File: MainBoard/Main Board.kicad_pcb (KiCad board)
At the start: 2 copper layers, 120 x 107 mm, 33 parts, among them IC1 TLV61070ADBVR, J1 Motor, J2 Motor, J3 Row 2, J4 Row 2, J8 Conn_01x16_Pin, Q1 NMOS, Q2 NMOS, U1 TP4056, U2 DW01A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

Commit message: Small Changes to mainboard schematic
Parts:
- removed C1, C2: 220u, Capacitor_THT:CP_Radial_D8.0mm_P5.00mm
- removed D5, D6: D, Diode_THT:D_DO-15_P10.16mm_Horizontal
- removed IC1: TLV61070ADBVR, ImportedLibrary:TLV61070ADBVR
- removed J2: Motor, TerminalBlock:TerminalBlock_bornier-2_P5.08mm
- removed L1: 4u7, Inductor_SMD:L_6.3x6.3_H3
- removed Q1, Q2: NMOS, Package_TO_SOT_THT:TO-220F-3_Vertical
- removed R1, R4, R9: 100, Resistor_SMD:R_0402_1005Metric
- removed R10, R2: 10k, Resistor_SMD:R_0402_1005Metric
- removed U1: TP4056, Package_SO:SO-8_3.9x4.9mm_P1.27mm
- removed U2: DW01A, Package_TO_SOT_SMD:SOT-23-6
- removed U3: FS8205A, Package_TO_SOT_SMD:SOT-23-6

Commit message: Updated Mainboard
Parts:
- added C1: 220u, Capacitor_THT:CP_Radial_D8.0mm_P5.00mm, F.Cu at (40.6, 99.0)
- added C10: 3n3, Capacitor_SMD:C_0402_1005Metric, F.Cu at (43.6, 124.2)
- added C11: 10u, Capacitor_SMD:C_0603_1608Metric, F.Cu at (40.2, 119.6)
- added C12: 10u, Capacitor_SMD:C_0603_1608Metric, F.Cu at (40.2, 122.1)
- added C13: 10u, Capacitor_SMD:C_0603_1608Metric, F.Cu at (40.2, 124.6)
- added C14: 2n2, Capacitor_SMD:C_0402_1005Metric, F.Cu at (43.6, 126.1)
- added C15: 10u, Capacitor_SMD:C_0603_1608Metric, F.Cu at (40.2, 127.1)
- added C16: 10u, Capacitor_SMD:C_0603_1608Metric, F.Cu at (40.2, 129.6)
- added C2: 220u, Capacitor_THT:CP_Radial_D8.0mm_P5.00mm, F.Cu at (40.6, 108.6)
- added C3: 100n, Capacitor_SMD:C_0402_1005Metric, F.Cu at (43.6, 114.3)
- added C4: 100n, Capacitor_SMD:C_0402_1005Metric, F.Cu at (43.6, 116.3)
- added C5: 10u, Capacitor_SMD:C_0603_1608Metric, F.Cu at (40.2, 114.6)
- added C6: 100n, Capacitor_SMD:C_0402_1005Metric, F.Cu at (43.6, 118.3)
- added C7: 10u, Capacitor_SMD:C_0603_1608Metric, F.Cu at (40.2, 117.1)
- added C8: 1u, Capacitor_SMD:C_0402_1005Metric, F.Cu at (43.6, 120.2)
- added C9: 100n, Capacitor_SMD:C_0402_1005Metric, F.Cu at (43.6, 122.2)
- added D1: LED, LED_SMD:LED_0603_1608Metric, F.Cu at (73.6, 95.5)
- added D2: LED, LED_SMD:LED_0603_1608Metric, F.Cu at (73.6, 98.1)
- added D3: PMEG2010AEH, Diode_SMD:D_SOD-123F, F.Cu at (71.0, 116.2)
- added D4: PMEG2010AEH, Diode_SMD:D_SOD-123F, F.Cu at (71.0, 119.6)
- added D5: PMEG2010AEH, Diode_SMD:D_SOD-123F, F.Cu at (71.0, 122.9)
- added D6: PMEG2010AEH, Diode_SMD:D_SOD-123F, F.Cu at (71.0, 126.3)
- added IC1: TLV61070ADBVR, ImportedLibrary:TLV61070ADBVR, F.Cu at (44.8, 129.4)
- added J2: Motor, TerminalBlock:TerminalBlock_bornier-2_P5.08mm, F.Cu at (51.1, 119.1)
- added J5: USB PowerOnly 6P, Connector_USB:USB_C_Receptacle_GCT_USB4125-xx-x_6P_TopMnt_Horizontal, F.Cu at (65.6, 99.1)
- added L1: 6u8, Inductor_SMD:L_6.3x6.3_H3, F.Cu at (63.7, 128.4)
- added L2: 2u2, Inductor_SMD:L_Changjiang_FNR5030S, F.Cu at (73.5, 110.1)
- added Q1: NMOS, Package_TO_SOT_THT:TO-220F-3_Vertical, F.Cu at (51.3, 98.1)
- added Q2: NMOS, Package_TO_SOT_THT:TO-220F-3_Vertical, F.Cu at (51.3, 104.3)
- added R1: 100, Resistor_SMD:R_0402_1005Metric, F.Cu at (60.9, 115.5)
- added R10: 10k, Resistor_SMD:R_0402_1005Metric, F.Cu at (63.8, 123.5)
- added R11: R, Resistor_SMD:R_0402_1005Metric, F.Cu at (66.7, 115.5)
- added R12: R, Resistor_SMD:R_0402_1005Metric, F.Cu at (66.7, 117.5)
- added R13: 90k, Resistor_SMD:R_0402_1005Metric, F.Cu at (66.7, 119.5)
- added R14: 10k, Resistor_SMD:R_0402_1005Metric, F.Cu at (66.7, 121.5)
- added R2: 10k, Resistor_SMD:R_0402_1005Metric, F.Cu at (60.9, 117.5)
- added R3: 1k2, Resistor_SMD:R_0402_1005Metric, F.Cu at (60.9, 119.5)
- added R4: 100, Resistor_SMD:R_0402_1005Metric, F.Cu at (60.9, 121.5)
- added R5: 1k, Resistor_SMD:R_0402_1005Metric, F.Cu at (60.9, 123.5)
- added R6: 1k2, Resistor_SMD:R_0402_1005Metric, F.Cu at (63.8, 115.5)
- added R7: 1k2, Resistor_SMD:R_0402_1005Metric, F.Cu at (63.8, 117.5)
- added R8: 24k, Resistor_SMD:R_0402_1005Metric, F.Cu at (63.8, 119.5)
- added R9: 100, Resistor_SMD:R_0402_1005Metric, F.Cu at (63.8, 121.5)
- added RV1: R_Potentiometer, Potentiometer_SMD:Potentiometer_Bourns_TC33X_Vertical, F.Cu at (51.1, 126.0)
- added RV2: R_Potentiometer, Potentiometer_SMD:Potentiometer_Bourns_TC33X_Vertical, F.Cu at (51.1, 130.7)
- added SW1: SS12D10G5, ImportedLibrary:SS12D10G5_SlideSwitch, F.Cu at (54.8, 111.3)
- added U1: TP4056, Package_SO:SO-8_3.9x4.9mm_P1.27mm, F.Cu at (65.9, 110.0)
- added U2: DW01A, Package_TO_SOT_SMD:SOT-23-6, F.Cu at (56.6, 125.8)
- added U3: FS8205A, Package_TO_SOT_SMD:SOT-23-6, F.Cu at (56.6, 130.3)
- added U4: TPS61085DGK, Package_SO:VSSOP-8_3.0x3.0mm_P0.65mm, F.Cu at (72.2, 130.2)
- J8: value Conn_01x16_Pin -> FFC Connector
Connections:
- net /NANO_D10 renamed /PWM_L
- net /NANO_D9 renamed /PWM_R
- A1 pad 10: /NANO_D7 -> /IR_6_D
- A1 pad 11: /NANO_D8 -> /IR_7_D
- A1 pad 19: /NANO_A0 -> /IR_2_A
- A1 pad 20: /NANO_A1 -> /IR_3_A
- A1 pad 21: /NANO_A2 -> /IR_4_A
- A1 pad 22: /NANO_A3 -> /IR_5_A
- A1 pad 23: /NANO_A4 -> /IR_6_A
- A1 pad 30: +5V -> Net-(A1-VIN)
- A1 pad 5: /NANO_D2 -> /IR_1_D
- A1 pad 6: /NANO_D3 -> /IR_2_D
- A1 pad 7: /NANO_D4 -> /IR_3_D
- A1 pad 8: /NANO_D5 -> /IR_4_D
- A1 pad 9: /NANO_D6 -> /IR_5_D
- BT1 pad 1: +BATT -> Net-(BT1-+)
- BT1 pad 2: -BATT -> Net-(BT1--)
- J1 pad 1: VBUS -> Vdrive
- J3 pad 10: /NANO_D7 -> /IR_6_D
- J3 pad 11: /NANO_D8 -> /IR_7_D
- J3 pad 5: /NANO_D2 -> /IR_1_D
- J3 pad 6: /NANO_D3 -> /IR_2_D
- J3 pad 7: /NANO_D4 -> /IR_3_D
- J3 pad 8: /NANO_D5 -> /IR_4_D
- J3 pad 9: /NANO_D6 -> /IR_5_D
- J4 pad 15: +5V -> Net-(A1-VIN)
- J4 pad 4: /NANO_A0 -> /IR_2_A
- J4 pad 5: /NANO_A1 -> /IR_3_A
- J4 pad 6: /NANO_A2 -> /IR_4_A
- J4 pad 7: /NANO_A3 -> /IR_5_A
- J4 pad 8: /NANO_A4 -> /IR_6_A

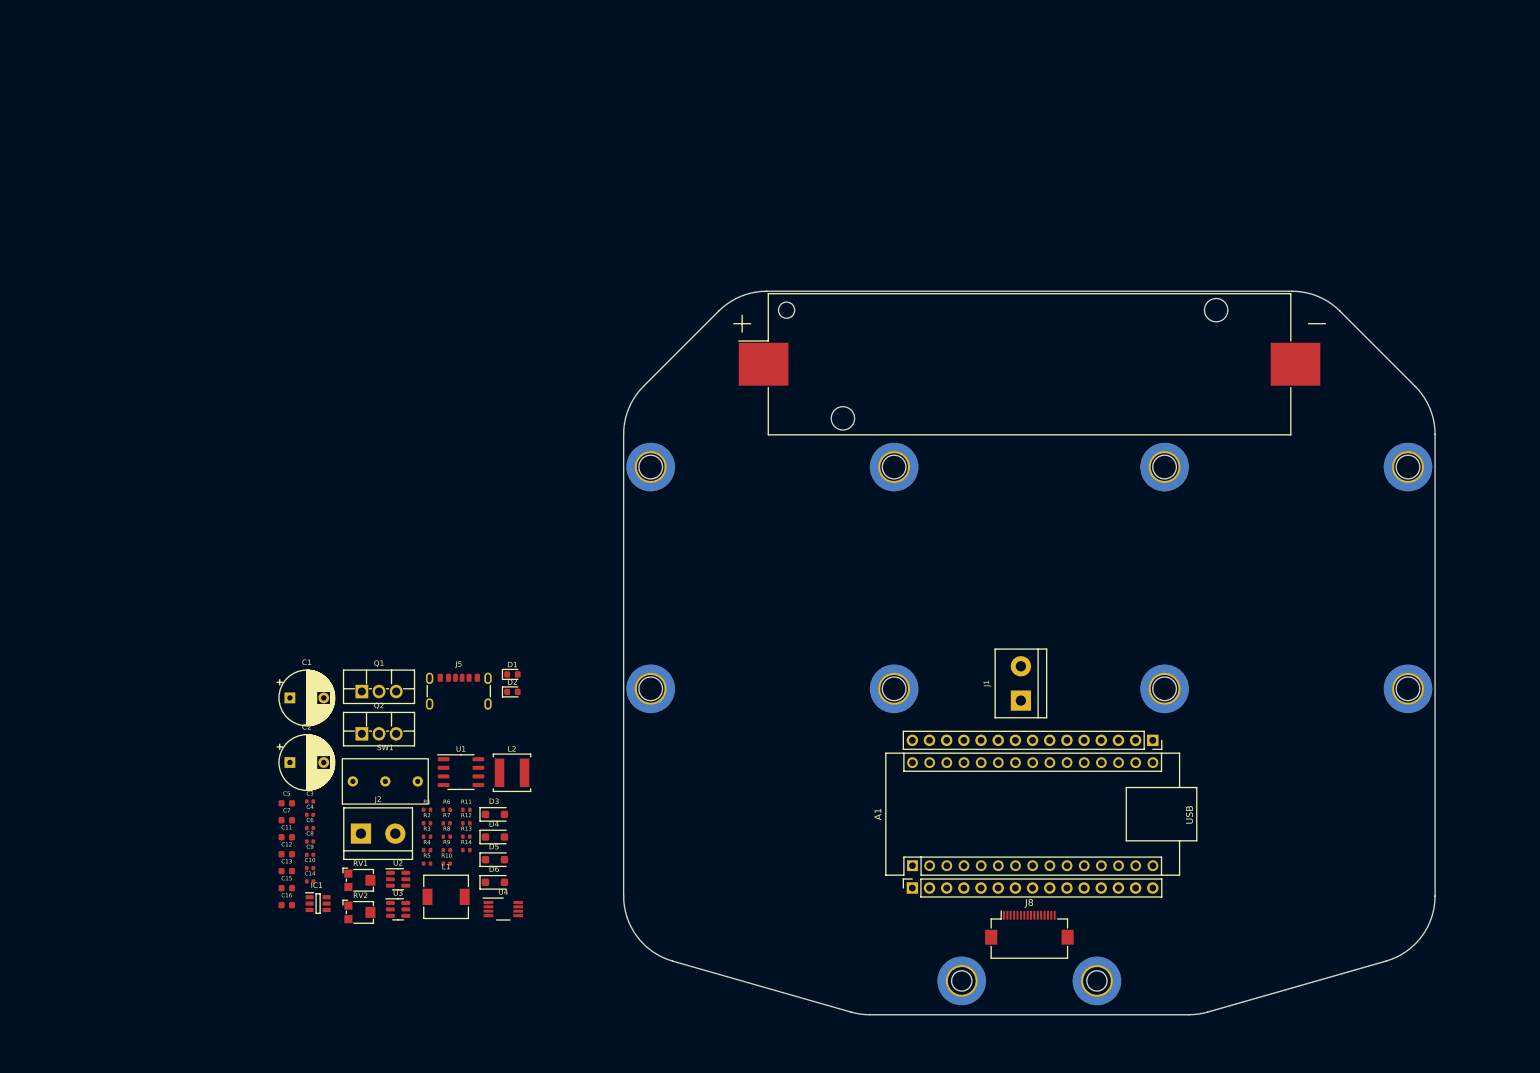
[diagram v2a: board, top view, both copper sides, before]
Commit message: Main board pcb traced
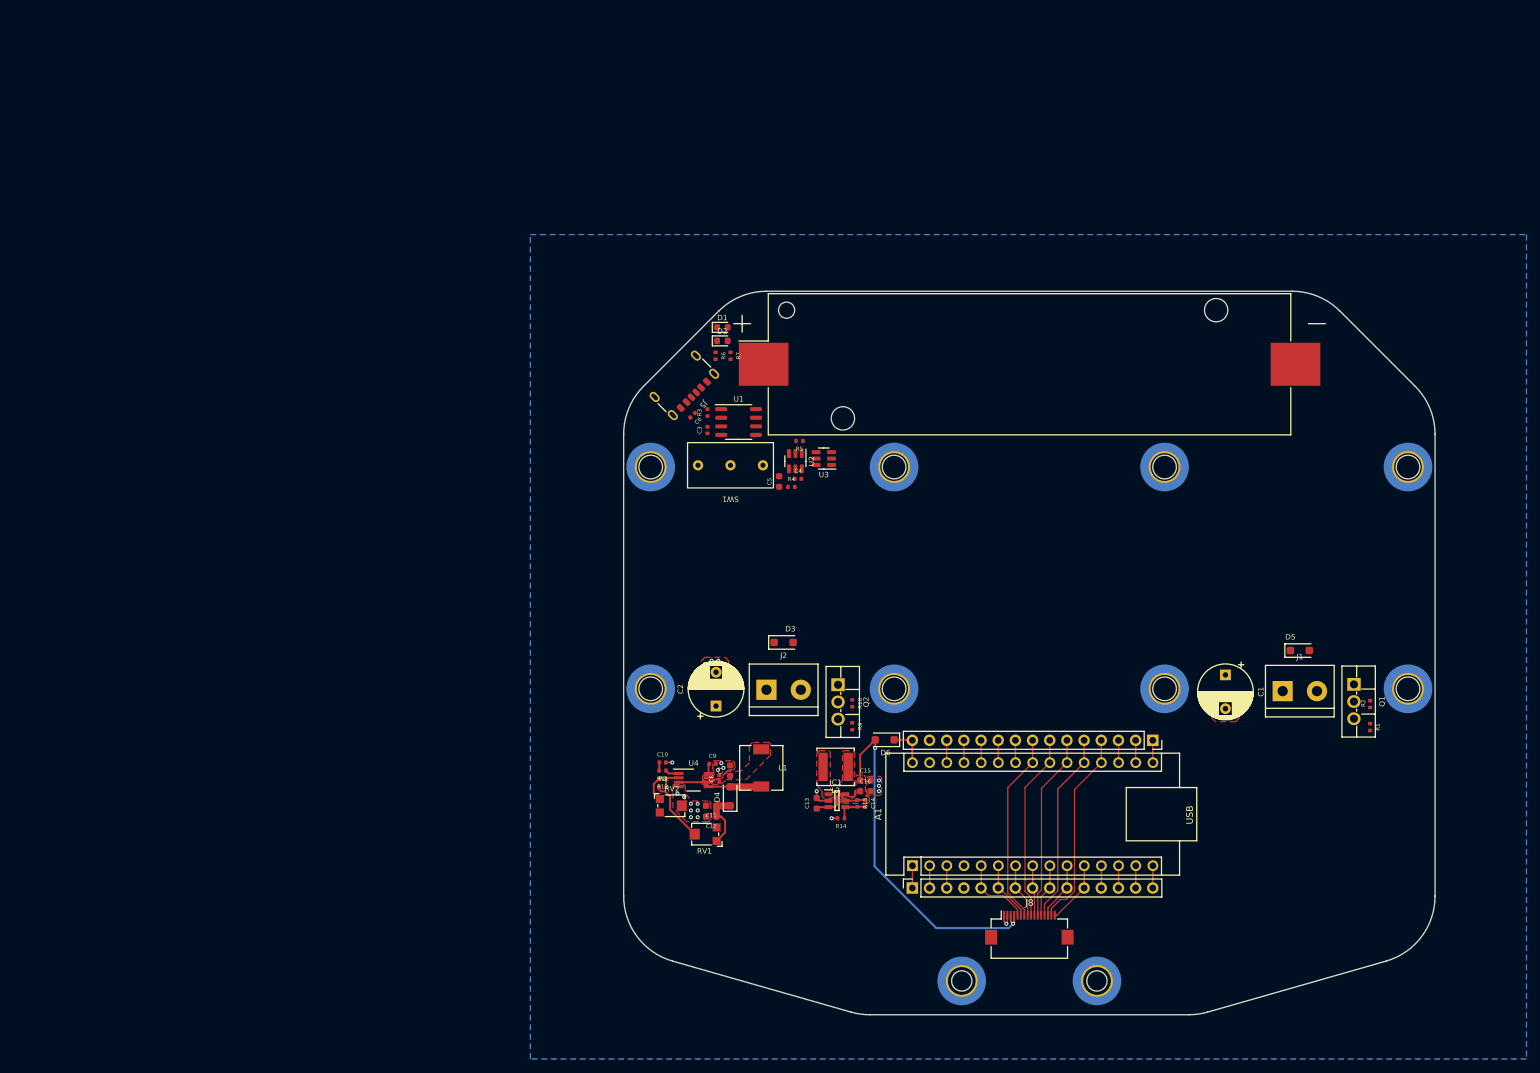
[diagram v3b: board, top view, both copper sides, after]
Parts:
- moved Q1 146.7 mm to (198.0, 97.0), turned to -90 degrees
- moved R2 140.6 mm to (200.4, 99.9), turned to -90 degrees
- moved R1 140.0 mm to (200.4, 103.3), turned to -90 degrees
- moved C1 138.4 mm to (179.0, 95.6), turned to -90 degrees
- moved D5 123.0 mm to (190.0, 92.0)
- moved U3 91.7 mm to (119.6, 63.6), turned to 180 degrees
- moved C4 87.6 mm to (115.8, 66.6)
- moved C16 87.2 mm to (125.8, 112.8)
- moved C15 87.0 mm to (125.8, 111.2)
- moved C5 87.0 mm to (113.0, 67.0), turned to 90 degrees
- moved U2 85.3 mm to (115.4, 64.0), turned to -90 degrees
- moved R5 83.3 mm to (116.0, 61.0), turned to 180 degrees
- moved C6 83.2 mm to (100.2, 57.2), turned to -135 degrees
- moved C14 82.9 mm to (125.8, 114.6), turned to -90 degrees
- moved R7 80.9 mm to (105.8, 48.4), turned to -90 degrees
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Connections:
- A1 pad 10: /IR_6_D -> /IR_2_D
- A1 pad 11: /IR_7_D -> /IR_1_D
- A1 pad 5: /IR_1_D -> /IR_7_D
- A1 pad 6: /IR_2_D -> /IR_6_D
- A1 pad 7: /IR_3_D -> /IR_5_D
- A1 pad 9: /IR_5_D -> /IR_3_D
- C10 pad 2: Net-(U4-FREQ) -> GND
- C7 pad 2: Net-(U4-FREQ) -> GND
- C8 pad 2: Net-(U4-FREQ) -> GND
- C9 pad 2: Net-(U4-FREQ) -> GND
- J3 pad 10: /IR_6_D -> /IR_2_D
- J3 pad 11: /IR_7_D -> /IR_1_D
- J3 pad 5: /IR_1_D -> /IR_7_D
- J3 pad 6: /IR_2_D -> /IR_6_D
- J3 pad 7: /IR_3_D -> /IR_5_D
- J3 pad 9: /IR_5_D -> /IR_3_D
- Q1 pad 1: Net-(D5-A) -> Net-(Q1-G)
- Q1 pad 2: Net-(Q1-G) -> Net-(D5-A)
- Q2 pad 1: Net-(D3-A) -> Net-(Q2-G)
- Q2 pad 2: Net-(Q2-G) -> Net-(D3-A)
- U3 pad 2: (no net) -> Net-(BT1--)
- U3 pad 3: (no net) -> Net-(BT1--)
- U3 pad 6: (no net) -> GND
- U4 pad 4: Net-(U4-FREQ) -> GND
- U4 pad 7: Net-(U4-FREQ) -> GND
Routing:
- net +5V: track 0.00 -> 55.9 mm, vias 0 -> 2
- net /IR_2_A: track 0.00 -> 29.5 mm
- net /IR_6_A: track 0.00 -> 28.4 mm
- net /IR_3_A: track 0.00 -> 28.3 mm
- net /IR_5_A: track 0.00 -> 27.8 mm
- net /IR_4_A: track 0.00 -> 27.7 mm
- net /IR_7_D: track 0.00 -> 10.9 mm
- net VBUS: track 0.00 -> 10.2 mm
- net Net-(R11-Pad1): track 0.00 -> 9.53 mm
- net /IR_1_D: track 0.00 -> 9.33 mm
- net /IR_6_D: track 0.00 -> 8.83 mm
- net Vdrive: track 0.00 -> 8.67 mm
- net /IR_2_D: track 0.00 -> 8.51 mm
- net /IR_5_D: track 0.00 -> 8.10 mm
- net /IR_3_D: track 0.00 -> 7.87 mm
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- added copper zone on F.Cu, net +5V
- added copper zone on B.Cu, net GND
- added copper zone on F.Cu, net GND
- added copper zone on F.Cu, net Net-(IC1-SW)
- added copper zone on F.Cu, net VBUS

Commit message: progressed on main board
Made some more connections. Not fully finished it, but added it for completeness
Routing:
- net Net-(BT1--): track 0.00 -> 76.4 mm
- net /PWM_R: track 3.31 -> 61.3 mm
- net /PWM_L: track 3.31 -> 48.8 mm
- net VCC: track 0.00 -> 32.2 mm
- net Vdrive: track 8.67 -> 40.5 mm
- net Net-(BT1-+): track 0.00 -> 20.0 mm
- net VBUS: track 10.2 -> 24.8 mm
- net Net-(D3-A): track 0.00 -> 13.7 mm
- net /STDBY: track 0.00 -> 13.4 mm, vias 0 -> 2
- net Net-(D5-A): track 0.00 -> 12.6 mm
- net /CHRG: track 0.00 -> 11.0 mm, vias 0 -> 2
- net Net-(Q1-G): track 0.00 -> 8.62 mm
- net Net-(Q2-G): track 0.00 -> 7.05 mm
- net GND: track 7.50 -> 14.1 mm, vias 38 -> 57
- net Net-(U2-OC): track 0.00 -> 4.89 mm
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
